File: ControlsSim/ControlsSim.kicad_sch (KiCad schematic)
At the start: 0 parts

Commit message: Initial schematic with parts
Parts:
- added D?: Arr_Cntctr_Main, LED_SMD:LED_0805_2012Metric, symbol Device:LED
- added D?: Arr_Cntctr_PreChg, LED_SMD:LED_0805_2012Metric, symbol Device:LED
- added D?: M_Cntctr_Main, LED_SMD:LED_0805_2012Metric, symbol Device:LED
- added D?: KillSw_Ind, LED_SMD:LED_0805_2012Metric, symbol Device:LED
- added D?: M_Cntctr_PreChg, LED_SMD:LED_0805_2012Metric, symbol Device:LED
- added J?: Accel_Pots, Connector_Molex:Molex_Micro-Fit_3.0_43045-0612_2x03_P3.00mm_Vertical, symbol Connector_Generic:Conn_02x03_Top_Bottom
- added J?: Minion Passthrough In, Connector_Molex:Molex_Micro-Fit_3.0_43045-1012_2x05_P3.00mm_Vertical, symbol Connector_Generic:Conn_02x05_Top_Bottom
- added J?: Conn_01x02, UTSVT_Connectors:Molex_MicroFit3.0_1x2xP3.00mm_PolarizingPeg_Vertical, symbol Connector_Generic:Conn_01x02
- added J?: DisplayConn, Connector_PinHeader_2.54mm:PinHeader_1x04_P2.54mm_Vertical, symbol Connector_Generic:Conn_01x04
- added J?: CAN, UTSVT_Connectors:Molex_MicroFit3.0_1x2xP3.00mm_PolarizingPeg_Vertical, symbol Connector_Generic:Conn_01x02
- added J?: Brake_Pots, Connector_Molex:Molex_Micro-Fit_3.0_43045-0612_2x03_P3.00mm_Vertical, symbol Connector_Generic:Conn_02x03_Top_Bottom
- added J?: KillSw, UTSVT_Connectors:Molex_MicroFit3.0_1x2xP3.00mm_PolarizingPeg_Vertical, symbol Connector_Generic:Conn_01x02
- added J?: Motor Contactors, Connector_Molex:Molex_Micro-Fit_3.0_43650-0415_1x04_P3.00mm_Vertical, symbol Connector_Generic:Conn_01x04
- added J?: Array Contactors, Connector_Molex:Molex_Micro-Fit_3.0_43650-0415_1x04_P3.00mm_Vertical, symbol Connector_Generic:Conn_01x04
- added J?: Conn_01x14, Connector_Molex:Molex_Micro-Fit_3.0_43045-1412_2x07_P3.00mm_Vertical, symbol Connector_Generic:Conn_01x14
- added J?: Minion Passthrough Out, Connector_Molex:Molex_Micro-Fit_3.0_43045-1012_2x05_P3.00mm_Vertical, symbol Connector_Generic:Conn_02x05_Top_Bottom
- added J?: CANable, symbol Connector:Screw_Terminal_01x03
- added R? (x2): 1.5k, symbol Device:R_Small
- added R? (x2): 1k, symbol Device:R_Small
- added RV?: Accel_Pot2, symbol Device:R_Potentiometer
- added RV?: Brake_Pot1, symbol Device:R_Potentiometer
- added RV?: Brake_Pot2, symbol Device:R_Potentiometer
- added RV?: Accel_Pot1, symbol Device:R_Potentiometer
- added SW?: SW_Rotary2x6, symbol Switch:SW_Rotary2x6
- added SW?: KillSw, symbol Switch:SW_SPST
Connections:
- new net: D?.1 (K), R?.1 (x3)
- new net: J?.1 (Pin_1), RV?.1 (x2)
- new net: J?.2 (Pin_2), RV?.2 (x2)
- new net: J?.3 (Pin_3), RV?.3 (x2)
- new net: J?.4 (Pin_4), RV?.3 (x2)
- new net: J?.5 (Pin_5), RV?.2 (x2)
- new net: J?.6 (Pin_6), RV?.1 (x2)
- new net: J?.3 (Pin_3), R?.2
- new net: J?.1 (Pin_1), SW?.1
- new net: J?.10 (Pin_10), SW?.10
- new net: J?.11 (Pin_11), SW?.11
- new net: J?.2 (Pin_2), SW?.2
- new net: J?.3 (Pin_3), SW?.3
- new net: J?.4 (Pin_4), SW?.4
- new net: J?.5 (Pin_5), SW?.5
- new net: J?.7 (Pin_7), SW?.7
- new net: J?.8 (Pin_8), SW?.8
- new net: J?.9 (Pin_9), SW?.9
- new net: D?.1 (K), J?.1 (Pin_1)
- new net: D?.2 (A), J?.2 (Pin_2)
- new net: J?.1 (Pin_1), SW?.2 (B)
- new net: J?.1 (Pin_1), R?.2 (x2)
- new net: J?.3 (Pin_3), R?.1
- new net: D?.1 (K), R?.2
- new net +12V: J?.13 (Pin_13), J?.14 (Pin_14), SW?.13, SW?.14
- new net +5V: D?.2 (A), D?.2 (A), D?.2 (A), D?.2 (A), J?.1 (Pin_1), J?.1 (Pin_1), J?.1 (Pin_1), SW?.1 (A)
- new net CANH: J?.1 (Pin_1), J?.2 (Pin_2)
- new net CANL: J?.2 (Pin_2), J?.3 (Pin_3)
- new net CAN_GND: J?.1 (Pin_1)
- new net CLK: J?.8 (Pin_8), J?.8 (Pin_8)
- new net CS: J?.9 (Pin_9), J?.9 (Pin_9)
- new net GND: J?.2 (Pin_2), J?.2 (Pin_2), J?.2 (Pin_2), J?.2 (Pin_2), J?.2 (Pin_2), J?.4 (Pin_4), J?.4 (Pin_4), J?.4 (Pin_4)
- new net MISO: J?.4 (Pin_4), J?.4 (Pin_4)
- new net MOSI: J?.3 (Pin_3), J?.3 (Pin_3)
- new net UART_Rx: J?.3 (Pin_3), J?.7 (Pin_7)
- new net UART_Tx: J?.2 (Pin_2), J?.6 (Pin_6)
- no-connect marks 0 -> 9
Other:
- note added: "No BPS PWR connection(?)"

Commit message: Revised schematic with input from Babu, intial PCB layout
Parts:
- removed D?: KillSw_Ind, LED_SMD:LED_0805_2012Metric, symbol Device:LED
- removed J?: Conn_01x02, UTSVT_Connectors:Molex_MicroFit3.0_1x2xP3.00mm_PolarizingPeg_Vertical, symbol Connector_Generic:Conn_01x02
- removed J?: CAN, UTSVT_Connectors:Molex_MicroFit3.0_1x2xP3.00mm_PolarizingPeg_Vertical, symbol Connector_Generic:Conn_01x02
- removed J?: KillSw, UTSVT_Connectors:Molex_MicroFit3.0_1x2xP3.00mm_PolarizingPeg_Vertical, symbol Connector_Generic:Conn_01x02
- removed J?: CANable, symbol Connector:Screw_Terminal_01x03
- removed R?: 1k, symbol Device:R_Small
- removed SW?: KillSw, symbol Switch:SW_SPST
- added H1: Display Mounting Holes, MountingHole:MountingHole_3.2mm_M3, symbol Mechanical:MountingHole
- added R2: 1k, Resistor_SMD:R_0805_2012Metric, symbol Device:R_Small
- D1, D2: renamed from D?; MFG PN (none) -> APTD2012LVBC/D
- R1: renamed from R?; footprint (none) -> Resistor_SMD:R_0805_2012Metric; MFR Part # (none) -> CRCW08051K00FKEAC
- R3, R4: renamed from R?; footprint (none) -> Resistor_SMD:R_0805_2012Metric
- RV1, RV2, RV3, RV4: renamed from RV?; footprint (none) -> Footprints:PTA4543
- SW2: renamed from SW?; footprint (none) -> Footprints:CK1035
- gave numbers to parts that had none: 10
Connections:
- net A_D_Mn1: now reaches D3.1 (K), R3.1
- net A_D_Pre1: now reaches D4.1 (K), R4.1
- net M_D_Mn1: now reaches D1.1 (K), R1.1
- net Acc_Pot1_V+: now reaches J2.1 (Pin_1), RV1.1
- net Acc_Pot1_Vo: now reaches J2.2 (Pin_2), RV1.2
- net Acc_Pot1_Gnd: now reaches J2.3 (Pin_3), RV1.3
- net Acc_Pot2_V+: now reaches J2.4 (Pin_4), RV3.3
- net Acc_Pot2_Vo: now reaches J2.5 (Pin_5), RV3.2
- net Acc_Pot2_Gnd: now reaches J2.6 (Pin_6), RV3.1
- net A_D_Pre2: now reaches J6.3 (Pin_3), R4.2
- net Rot1: now reaches J7.1 (Pin_1), SW2.1
- net Rot10: now reaches J7.10 (Pin_10), SW2.10
- net Rot11: now reaches J7.11 (Pin_11), SW2.11
- net Rot2: now reaches J7.2 (Pin_2), SW2.2
- net Rot3: now reaches J7.3 (Pin_3), SW2.3
- net Rot4: now reaches J7.4 (Pin_4), SW2.4
- net Rot5: now reaches J7.5 (Pin_5), SW2.5
- net Rot7: now reaches J7.7 (Pin_7), SW2.7
- net Rot8: now reaches J7.8 (Pin_8), SW2.8
- net Rot9: now reaches J7.9 (Pin_9), SW2.9
- net Brk_Pot1_V+: now reaches J3.1 (Pin_1), RV2.1
- net Brk_Pot1_Vo: now reaches J3.2 (Pin_2), RV2.2
- net Brk_Pot1_Gnd: now reaches J3.3 (Pin_3), RV2.3
- net BPS_PWR: now reaches J8.5 (Pin_5)
- net BPS_PWR: now also J9.5 (Pin_5)
- net Brk_Pot2_Gnd: now reaches J3.6 (Pin_6), RV4.1
- net Brk_Pot2_Vo: now reaches J3.5 (Pin_5), RV4.2
- net Brk_Pot2_V+: now reaches J3.4 (Pin_4), RV4.3
- net M_D_Mn2: now reaches J5.1 (Pin_1), R1.2
- net M_D_Pre2: now reaches J5.3 (Pin_3)
- net M_D_Pre2: now also R2.1
- net A_D_Mn2: now reaches J6.1 (Pin_1), R3.2
- net M_D_Pre1: now reaches D2.1 (K)
- net M_D_Pre1: now also R2.2
- net +12V renamed RotV+
- no-connect marks 9 -> 8
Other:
- note removed: "No BPS PWR connection(?)"

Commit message: almost final PCB
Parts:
- removed RV2: Brake_Pot1, Footprints:PTA4543, symbol Device:R_Potentiometer
- removed RV3: Accel_Pot2, Footprints:PTA4543, symbol Device:R_Potentiometer
- removed RV4: Brake_Pot2, Footprints:PTA4543, symbol Device:R_Potentiometer
- added H2, H3: MountingHole, MountingHole:MountingHole_3.2mm_M3, symbol Mechanical:MountingHole
- added R5: 10k, Resistor_SMD:R_0805_2012Metric, symbol Device:R_Small
- added S1: Brake button, Footprints:TS16121295BK260SMTTR, symbol TS16-1212-95-BK-260-SMT-TR:TS16-1212-95-BK-260-SMT-TR
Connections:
- net Acc_Pot1_Gnd renamed Acc_Pot_Gnd
- net Acc_Pot1_V+ renamed Acc_Pot_V+
- net Acc_Pot1_Vo renamed Acc_Pot_Vo
- net Acc_Pot2_Gnd: no longer names the net of J2.6 (Pin_6)
- net Acc_Pot2_V+: no longer names the net of J2.4 (Pin_4)
- net Acc_Pot2_Vo: no longer names the net of J2.5 (Pin_5)
- net Brk_Pot1_Gnd renamed Brk_GND
- net Brk_GND: now also R5.2
- net Brk_Pot1_V+ renamed Brk_V+
- net Brk_V+: now also S1.2 (NO_2)
- net Brk_Pot1_Vo renamed Brk_Signal
- net Brk_Signal: now also R5.1, S1.4 (COM_2)
- net Brk_Pot2_Gnd: no longer names the net of J3.6 (Pin_6)
- net Brk_Pot2_V+: no longer names the net of J3.4 (Pin_4)
- net Brk_Pot2_Vo: no longer names the net of J3.5 (Pin_5)
- no-connect marks 8 -> 16

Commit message: added logos
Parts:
- added LOGO1: Hallock, UTSVT_Special:Hallock_Image_Small, symbol utsvt-misc:Logo_Placeholder
- added LOGO2: UTSVT Logo, UTSVT_Special:UTSVT_Logo_Symbol, symbol utsvt-misc:Logo_Placeholder
- J10: value DisplayConn -> Display
- J2: value Accel_Pots -> Accelerator Pot
- J3: value Brake_Pots -> Brake Button
- J7: value Conn_01x14 -> Rotary Switch
- RV1: value Accel_Pot1 -> Accelerator
- S1: value Brake button -> Brake
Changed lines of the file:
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@@
     (in_bom yes) (on_board yes)
     (property "Reference" "J2" (id 0) (at 77.47 119.38 0))
-    (property "Value" "Accel_Pots" (id 1) (at 77.47 121.92 0))
+    (property "Value" "Accelerator Pot" (id 1) (at 77.47 121.92 0))
     (property "Footprint" "Connector_Molex:Molex_Micro-Fit_3.0_43045-0612_2x03_P3.00mm_Vertical" (id 2) (at 76.2 127.635 0)
       (effects (font (size 1.27 1.27)) hide)
@@
     )
     (pin "1")
+  )
+  (symbol (lib_id "utsvt-misc:Logo_Placeholder") (at 223.52 130.175 0) (unit 1)
+    (in_bom yes) (on_board yes) (fields_autoplaced)
+    (property "Reference" "LOGO1" (id 0) (at 223.52 126.365 0)
+      (effects (font (size 1.27 1.27)) hide)
+    )
+    (property "Value" "Hallock" (id 1) (at 227.33 130.1749 0)
+      (effects (font (size 1.27 1.27)) (justify left))
+    )
+    (property "Footprint" "UTSVT_Special:Hallock_Image_Small" (id 2) (at 223.52 128.27 0)
+      (effects (font (size 1.27 1.27)) hide)
+    )
+    (property "Datasheet" "" (id 3) (at 223.52 128.27 0)
+      (effects (font (size 1.27 1.27)) hide)
+    )
   )
   (symbol (lib_id "Switch:SW_Rotary2x6") (at 182.88 60.96 180) (unit 1)
@@
     (in_bom yes) (on_board yes) (fields_autoplaced)
     (property "Reference" "S1" (id 0) (at 39.37 135.89 0))
-    (property "Value" "Brake button" (id 1) (at 39.37 138.43 0))
+    (property "Value" "Brake" (id 1) (at 39.37 138.43 0))
     (property "Footprint" "Footprints:TS16121295BK260SMTTR" (id 2) (at 50.8 140.97 0)
       (effects (font (size 1.27 1.27)) (justify left) hide)
@@
     (pin "4")
   )
+  (symbol (lib_id "utsvt-misc:Logo_Placeholder") (at 223.52 139.065 0) (unit 1)
+    (in_bom yes) (on_board yes) (fields_autoplaced)
+    (property "Reference" "LOGO2" (id 0) (at 223.52 135.255 0)
+      (effects (font (size 1.27 1.27)) hide)
+    )
+    (property "Value" "UTSVT Logo" (id 1) (at 227.33 139.0649 0)
+      (effects (font (size 1.27 1.27)) (justify left))
+    )
+    (property "Footprint" "UTSVT_Special:UTSVT_Logo_Symbol" (id 2) (at 223.52 137.16 0)
+      (effects (font (size 1.27 1.27)) hide)
+    )
+    (property "Datasheet" "" (id 3) (at 223.52 137.16 0)
+      (effects (font (size 1.27 1.27)) hide)
+    )
+  )
   (symbol (lib_id "Mechanical:MountingHole") (at 255.27 146.05 0) (unit 1)
     (in_bom yes) (on_board yes) (fields_autoplaced)
@@
       (effects (font (size 1.27 1.27)) (justify left))
     )
-    (property "Value" "DisplayConn" (id 1) (at 264.16 111.7599 0)
+    (property "Value" "Display" (id 1) (at 264.16 111.7599 0)
       (effects (font (size 1.27 1.27)) (justify left))
     )
@@
     (in_bom yes) (on_board yes)
     (property "Reference" "J3" (id 0) (at 77.47 135.255 0))
-    (property "Value" "Brake_Pots" (id 1) (at 77.47 137.795 0))
+    (property "Value" "Brake Button" (id 1) (at 77.47 137.795 0))
     (property "Footprint" "Connector_Molex:Molex_Micro-Fit_3.0_43045-0612_2x03_P3.00mm_Vertical" (id 2) (at 76.2 143.51 0)
       (effects (font (size 1.27 1.27)) hide)
@@
       (effects (font (size 1.27 1.27)) (justify right))
     )
-    (property "Value" "Accel_Pot1" (id 1) (at 50.8 128.9049 0)
+    (property "Value" "Accelerator" (id 1) (at 50.8 128.9049 0)
       (effects (font (size 1.27 1.27)) (justify right))
     )
@@
   (symbol (lib_id "Connector_Generic:Conn_01x14") (at 146.685 60.96 180) (unit 1)
     (in_bom yes) (on_board yes) (fields_autoplaced)
-    (property "Reference" "J7" (id 0) (at 143.51 60.9601 0)
-      (effects (font (size 1.27 1.27)) (justify left))
-    )
-    (property "Value" "Conn_01x14" (id 1) (at 143.51 58.4201 0)
-      (effects (font (size 1.27 1.27)) (justify left))
-    )
+    (property "Reference" "J7" (id 0) (at 146.685 36.83 0))
+    (property "Value" "Rotary Switch" (id 1) (at 146.685 39.37 0))
     (property "Footprint" "Connector_Molex:Molex_Micro-Fit_3.0_43045-1412_2x07_P3.00mm_Vertical" (id 2) (at 146.685 60.96 0)
       (effects (font (size 1.27 1.27)) hide)
@@
     )
     (path "/2fba5e1a-0ec2-4d0c-97a4-ae366ed2ecca"
-      (reference "J2") (unit 1) (value "Accel_Pots") (footprint "Connector_Molex:Molex_Micro-Fit_3.0_43045-0612_2x03_P3.00mm_Vertical")
+      (reference "J2") (unit 1) (value "Accelerator Pot") (footprint "Connector_Molex:Molex_Micro-Fit_3.0_43045-0612_2x03_P3.00mm_Vertical")
     )
     (path "/8d314573-a5ac-4fab-9c77-14e9875f3872"
-      (reference "J3") (unit 1) (value "Brake_Pots") (footprint "Connector_Molex:Molex_Micro-Fit_3.0_43045-0612_2x03_P3.00mm_Vertical")
+      (reference "J3") (unit 1) (value "Brake Button") (footprint "Connector_Molex:Molex_Micro-Fit_3.0_43045-0612_2x03_P3.00mm_Vertical")
     )
     (path "/c475e4a0-5393-42ac-9746-4f69ff30c5d0"
@@
     )
     (path "/d9171ac5-8d27-42a9-806c-2a53e86de5dc"
-      (reference "J7") (unit 1) (value "Conn_01x14") (footprint "Connector_Molex:Molex_Micro-Fit_3.0_43045-1412_2x07_P3.00mm_Vertical")
+      (reference "J7") (unit 1) (value "Rotary Switch") (footprint "Connector_Molex:Molex_Micro-Fit_3.0_43045-1412_2x07_P3.00mm_Vertical")
     )
     (path "/620050d0-bce2-483d-b892-048feefa5515"
@@
     )
     (path "/806198d2-d64d-46dd-b58c-db5d948d64bb"
-      (reference "J10") (unit 1) (value "DisplayConn") (footprint "Connector_PinHeader_2.54mm:PinHeader_1x04_P2.54mm_Vertical")
+      (reference "J10") (unit 1) (value "Display") (footprint "Connector_PinHeader_2.54mm:PinHeader_1x04_P2.54mm_Vertical")
+    )
+    (path "/48cdabb6-caeb-4b9b-a769-8648be617cc6"
+      (reference "LOGO1") (unit 1) (value "Hallock") (footprint "UTSVT_Special:Hallock_Image_Small")
+    )
+    (path "/726bdd88-fd57-41da-a291-42e6fb7de0a9"
+      (reference "LOGO2") (unit 1) (value "UTSVT Logo") (footprint "UTSVT_Special:UTSVT_Logo_Symbol")
     )
     (path "/bcc57875-8bcd-449e-bdac-51c2a40763fd"
@@
     )
     (path "/a47f5897-c300-41dd-af59-147e43c2f33a"
-      (reference "RV1") (unit 1) (value "Accel_Pot1") (footprint "Footprints:PTA4543")
+      (reference "RV1") (unit 1) (value "Accelerator") (footprint "Footprints:PTA4543")
     )
     (path "/70ef9f80-977b-4d2a-9ba6-14844876c2d9"
-      (reference "S1") (unit 1) (value "Brake button") (footprint "Footprints:TS16121295BK260SMTTR")
+      (reference "S1") (unit 1) (value "Brake") (footprint "Footprints:TS16121295BK260SMTTR")
     )
     (path "/4c8fc634-adb0-4373-b6a2-6ac587e3d6a4"

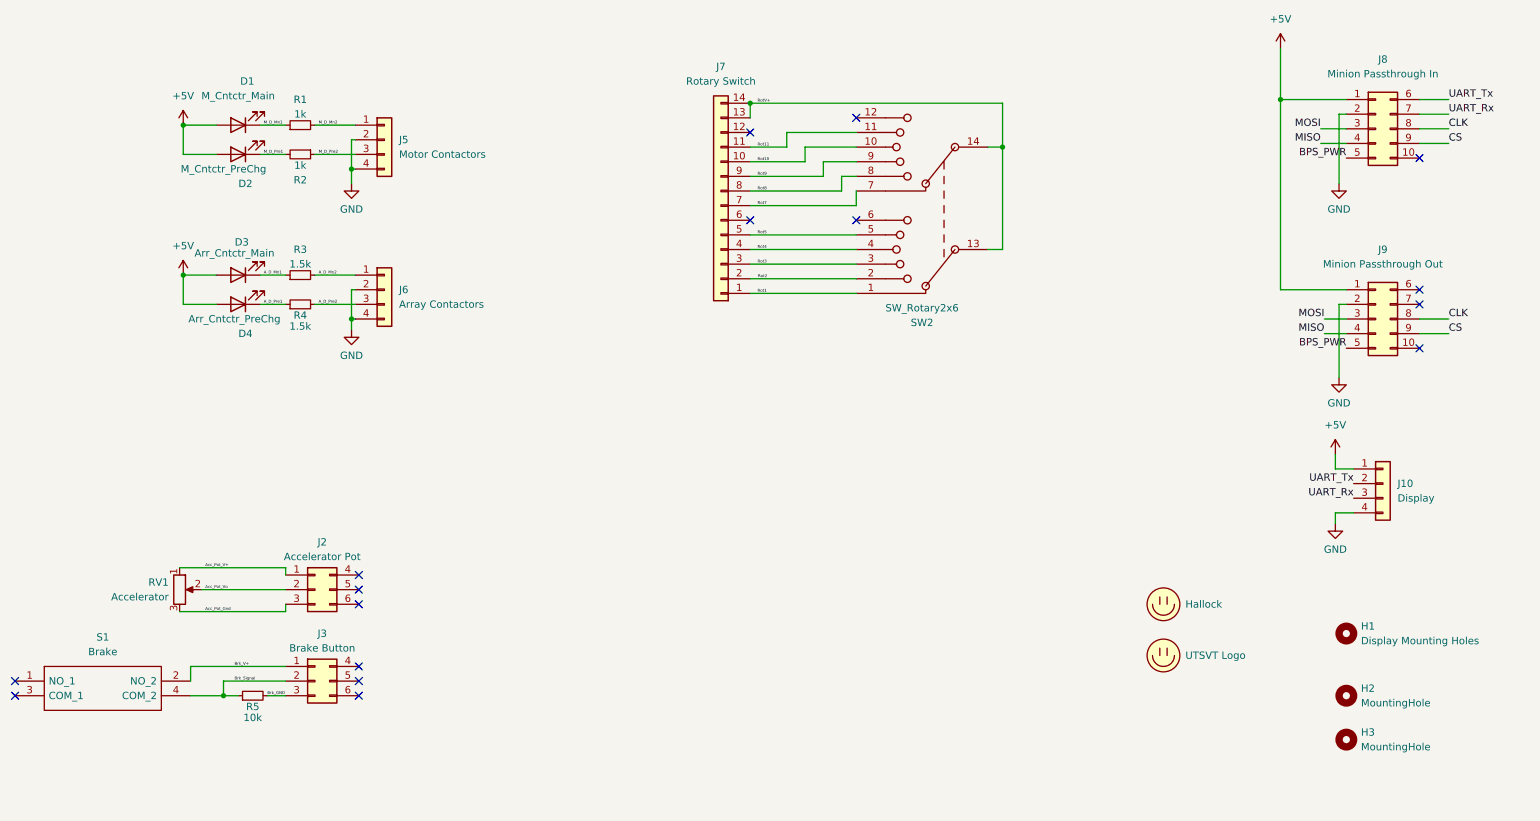
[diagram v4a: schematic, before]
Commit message: removed display connector
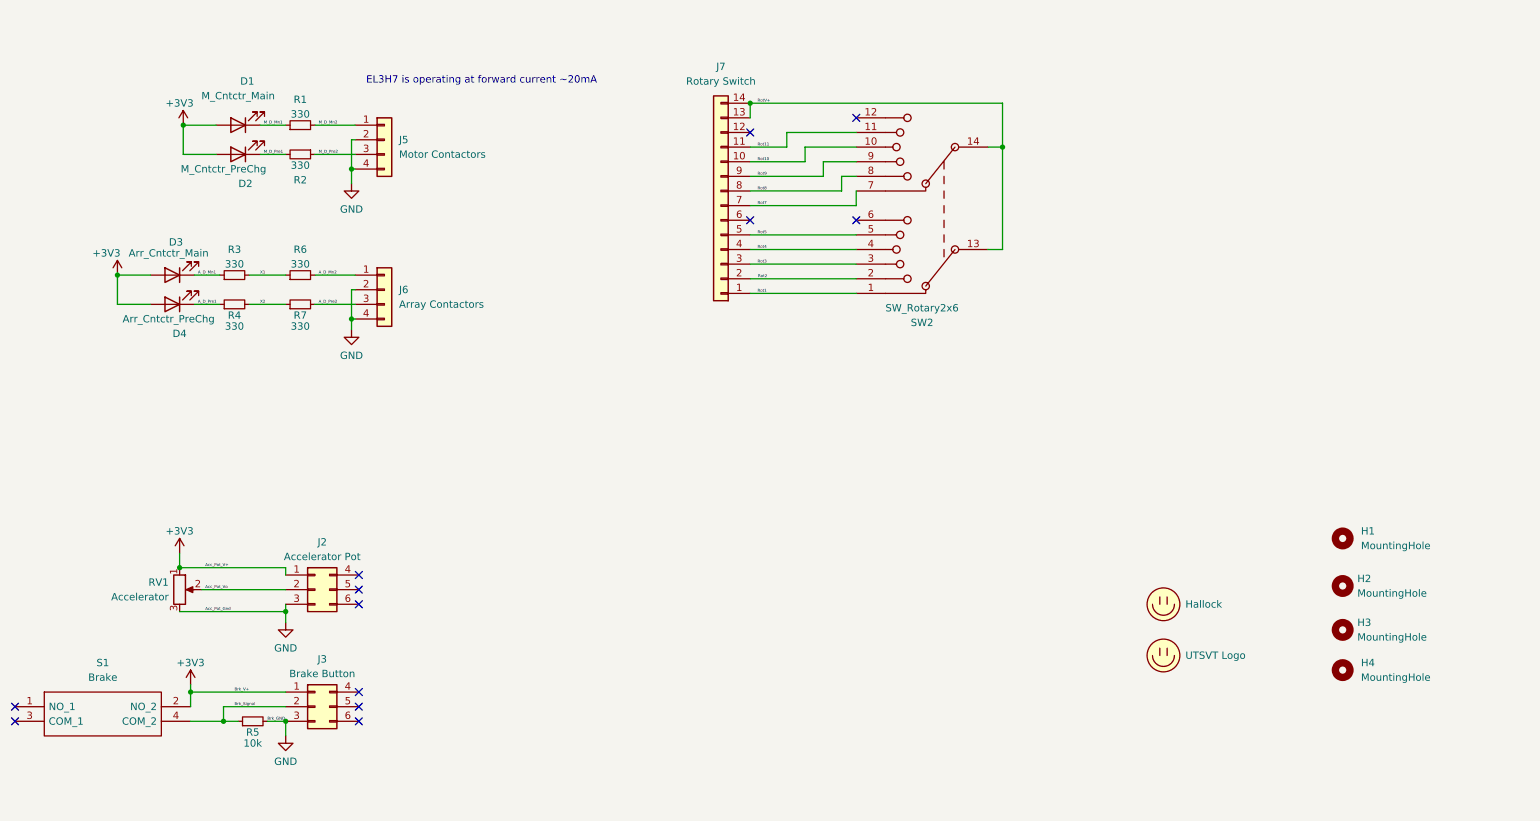
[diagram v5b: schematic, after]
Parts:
- removed J10: Display, Connector_PinHeader_2.54mm:PinHeader_1x04_P2.54mm_Vertical, symbol Connector_Generic:Conn_01x04
- removed J8: Minion Passthrough In, Connector_Molex:Molex_Micro-Fit_3.0_43045-1012_2x05_P3.00mm_Vertical, symbol Connector_Generic:Conn_02x05_Top_Bottom
- removed J9: Minion Passthrough Out, Connector_Molex:Molex_Micro-Fit_3.0_43045-1012_2x05_P3.00mm_Vertical, symbol Connector_Generic:Conn_02x05_Top_Bottom
- added H4: MountingHole, MountingHole:MountingHole_3.2mm_M3, symbol Mechanical:MountingHole
- added R6, R7: 330, Resistor_SMD:R_0805_2012Metric, symbol Device:R_Small
- H1: value Display Mounting Holes -> MountingHole
- R1, R2: value 1k -> 330; MFR Part # CRCW08051K00FKEAC -> (none)
- R3, R4: value 1.5k -> 330
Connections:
- net Acc_Pot_Gnd is gone; now on net GND: J2.3 (Pin_3), RV1.3
- net Acc_Pot_V+ is gone; now on net +3V3: J2.1 (Pin_1), RV1.1
- net Brk_GND is gone; now on net GND: J3.3 (Pin_3), R5.2
- net Brk_V+ is gone; now on net +3V3: J3.1 (Pin_1), S1.2 (NO_2)
- net A_D_Mn2: now also R6.2; no longer R3.2
- net A_D_Pre2: now also R7.2; no longer R4.2
- net +5V renamed +3V3
- new net X1: R3.2, R6.1
- new net X2: R4.2, R7.1
- no-connect marks 16 -> 12
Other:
- note added: "EL3H7 is operating at forward current ~20mA"
- moved on the sheet: D3, D4, H2, H3, J3, R3, R4, R5, S1
